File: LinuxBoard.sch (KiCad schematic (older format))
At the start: 0 parts

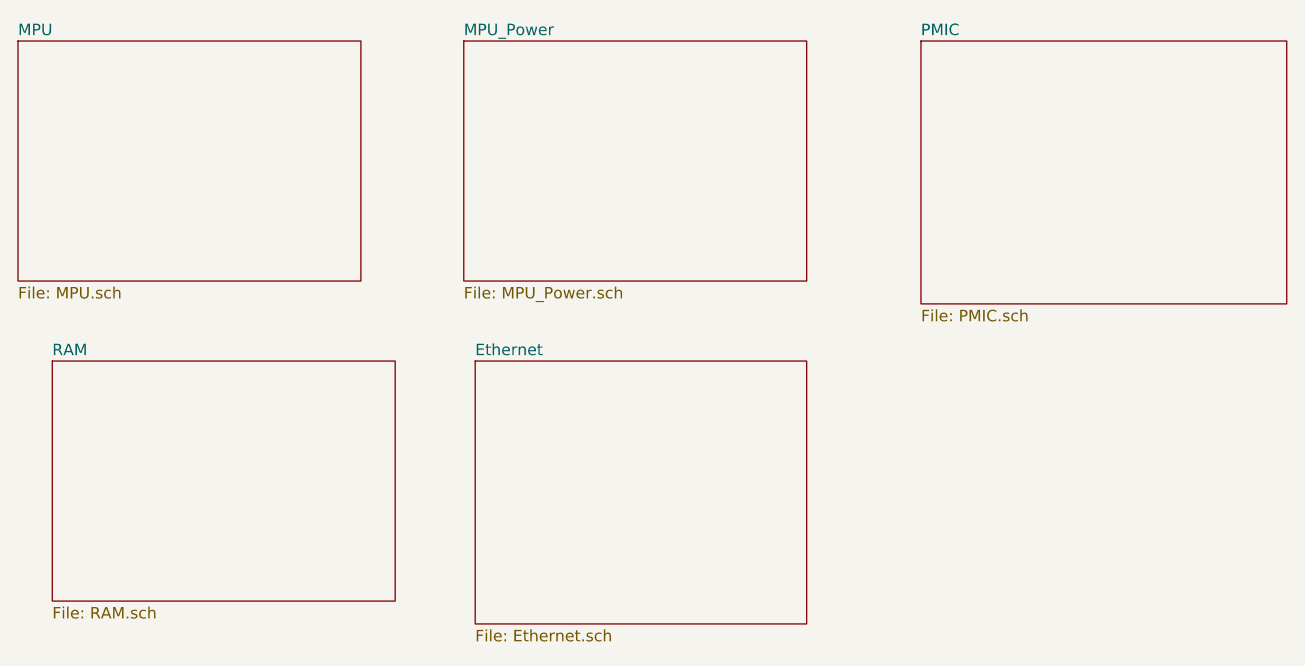
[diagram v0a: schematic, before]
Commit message: Complete ethernet and PMIC circuitry
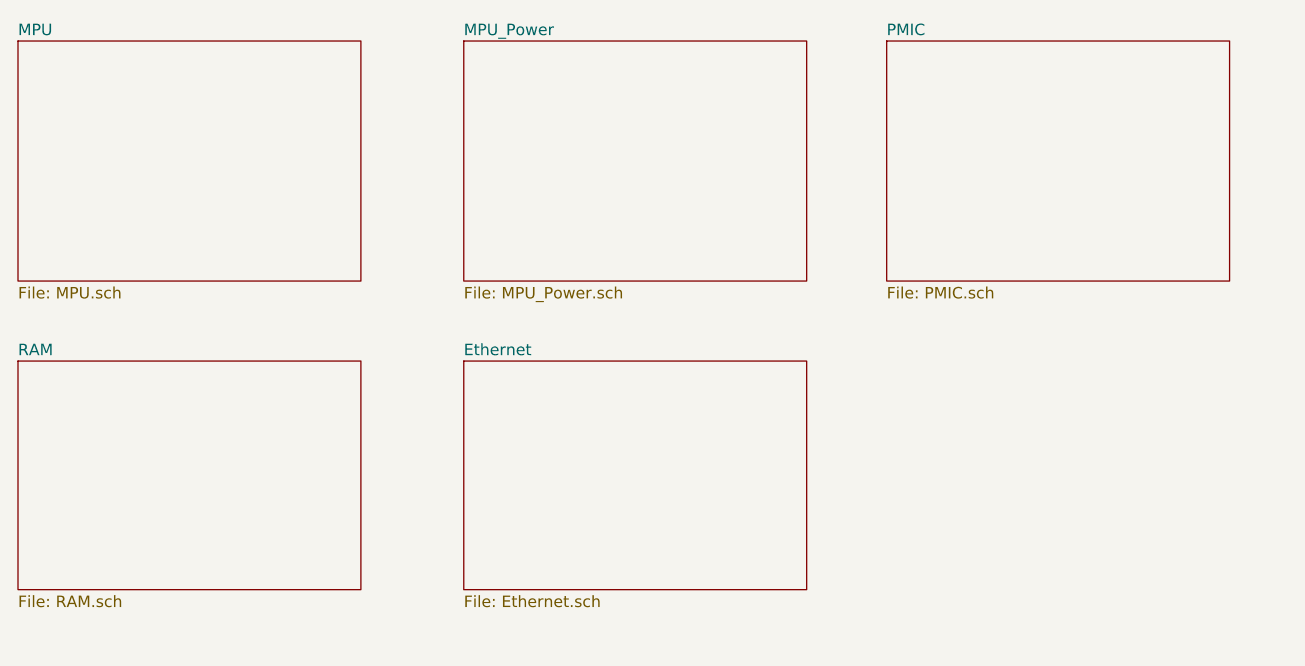
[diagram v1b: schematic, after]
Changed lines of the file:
@@
 $EndSheet
 $Sheet
-S 3300 3500 1500 1050
+S 3150 3500 1500 1000
 U 60172A77
 F0 "RAM" 50
@@
 $EndSheet
 $Sheet
-S 5150 3500 1450 1150
+S 5100 3500 1500 1000
 U 60172AD8
 F0 "Ethernet" 50
@@
 $EndSheet
 $Sheet
-S 7100 2100 1600 1150
+S 6950 2100 1500 1050
 U 60172B24
 F0 "PMIC" 50

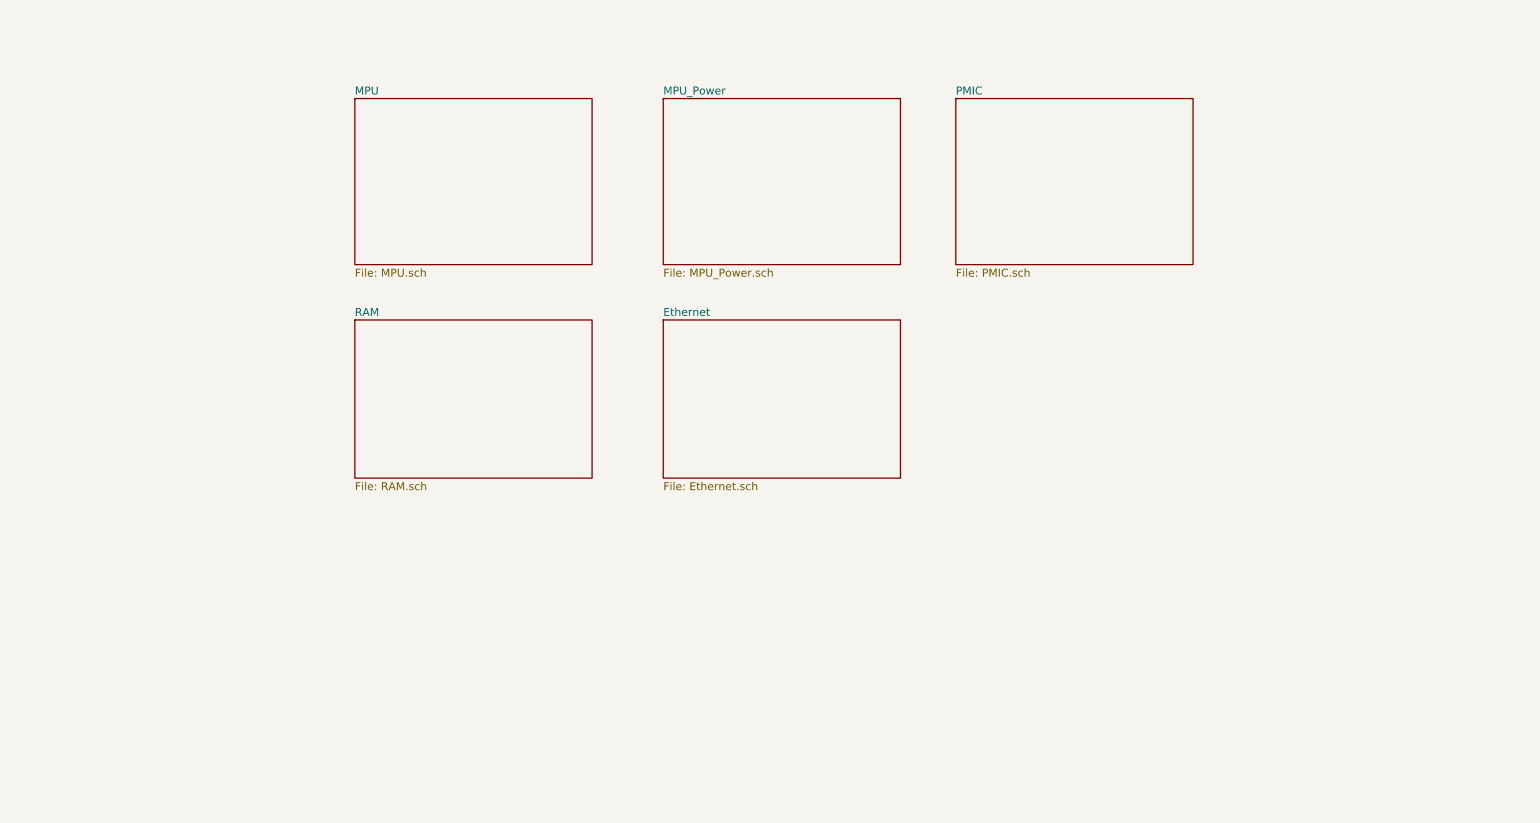
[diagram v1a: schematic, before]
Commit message: Complete gpio selection, tidy sheets
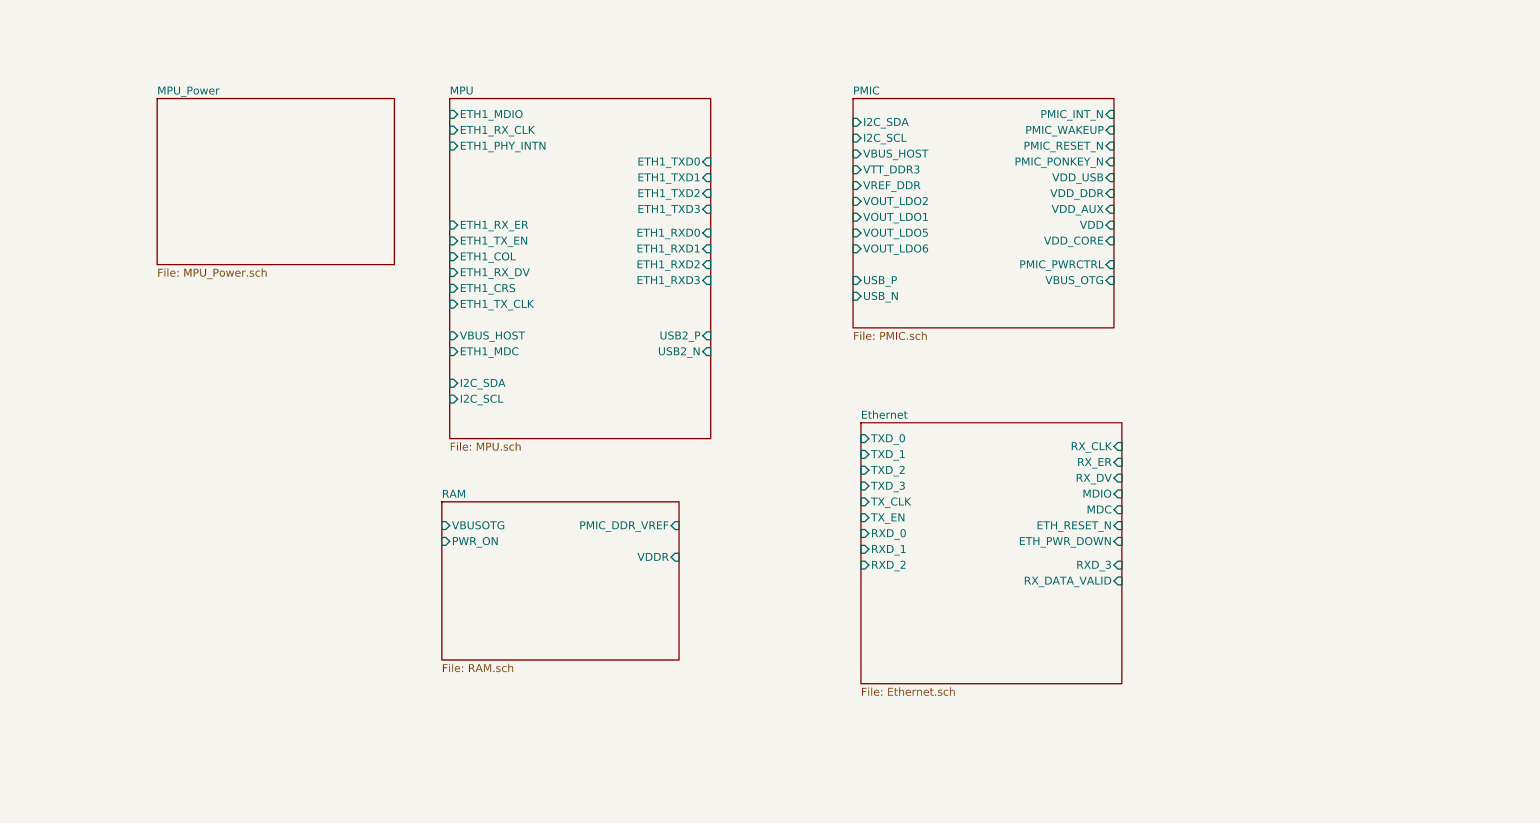
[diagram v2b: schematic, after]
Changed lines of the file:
@@
 $EndDescr
 $Sheet
-S 3150 2100 1500 1050
+S 3750 2100 1650 2150
 U 601728C0
 F0 "MPU" 50
 F1 "MPU.sch" 50
+F2 "ETH1_CRS" I L 3750 3300 50
+F3 "ETH1_RX_CLK" I L 3750 2300 50
+F4 "ETH1_MDIO" I L 3750 2200 50
+F5 "ETH1_COL" I L 3750 3100 50
+F6 "ETH1_RX_DV" I L 3750 3200 50
+F7 "ETH1_RXD2" I R 5400 3150 50
+F8 "ETH1_RXD3" I R 5400 3250 50
+F9 "ETH1_RX_ER" I L 3750 2900 50
+F10 "ETH1_TX_EN" I L 3750 3000 50
+F11 "ETH1_TXD1" I R 5400 2600 50
+F12 "ETH1_MDC" I L 3750 3700 50
+F13 "ETH1_TXD2" I R 5400 2700 50
+F14 "ETH1_TX_CLK" I L 3750 3400 50
+F15 "ETH1_RXD0" I R 5400 2950 50
+F16 "ETH1_RXD1" I R 5400 3050 50
+F17 "ETH1_TXD3" I R 5400 2800 50
+F18 "ETH1_PHY_INTN" I L 3750 2400 50
+F19 "ETH1_TXD0" I R 5400 2500 50
+F20 "I2C_SCL" I L 3750 4000 50
+F21 "I2C_SDA" I L 3750 3900 50
+F22 "VBUS_HOST" I L 3750 3600 50
+F23 "USB2_P" I R 5400 3600 50
+F24 "USB2_N" I R 5400 3700 50
 $EndSheet
 $Sheet
-S 5100 2100 1500 1050
+S 1900 2100 1500 1050
 U 601728E9
 F0 "MPU_Power" 50
@@
 $EndSheet
 $Sheet
-S 3150 3500 1500 1000
+S 3700 4650 1500 1000
 U 60172A77
 F0 "RAM" 50
 F1 "RAM.sch" 50
+F2 "VDDR" I R 5200 5000 50
+F3 "PMIC_DDR_VREF" I R 5200 4800 50
+F4 "PWR_ON" I L 3700 4900 50
+F5 "VBUSOTG" I L 3700 4800 50
 $EndSheet
 $Sheet
-S 5100 3500 1500 1000
+S 6350 4150 1650 1650
 U 60172AD8
 F0 "Ethernet" 50
 F1 "Ethernet.sch" 50
+F2 "TXD_0" I L 6350 4250 50
+F3 "TXD_1" I L 6350 4350 50
+F4 "TXD_2" I L 6350 4450 50
+F5 "TXD_3" I L 6350 4550 50
+F6 "TX_CLK" I L 6350 4650 50
+F7 "TX_EN" I L 6350 4750 50
+F8 "RXD_0" I L 6350 4850 50
+F9 "RXD_1" I L 6350 4950 50
+F10 "RXD_2" I L 6350 5050 50
+F11 "RXD_3" I R 8000 5050 50
+F12 "RX_CLK" I R 8000 4300 50
+F13 "RX_ER" I R 8000 4400 50
+F14 "RX_DV" I R 8000 4500 50
+F15 "MDIO" I R 8000 4600 50
+F16 "MDC" I R 8000 4700 50
+F17 "ETH_RESET_N" I R 8000 4800 50
+F18 "ETH_PWR_DOWN" I R 8000 4900 50
+F19 "RX_DATA_VALID" I R 8000 5150 50
 $EndSheet
 $Sheet
-S 6950 2100 1500 1050
+S 6300 2100 1650 1450
 U 60172B24
 F0 "PMIC" 50
 F1 "PMIC.sch" 50
+F2 "I2C_SDA" I L 6300 2250 50
+F3 "I2C_SCL" I L 6300 2350 50
+F4 "VBUS_HOST" I L 6300 2450 50
+F5 "VTT_DDR3" I L 6300 2550 50
+F6 "VREF_DDR" I L 6300 2650 50
+F7 "VOUT_LDO2" I L 6300 2750 50
+F8 "VOUT_LDO1" I L 6300 2850 50
+F9 "VOUT_LDO5" I L 6300 2950 50
+F10 "VOUT_LDO6" I L 6300 3050 50
+F11 "VDD_CORE" I R 7950 3000 50
+F12 "VDD" I R 7950 2900 50
+F13 "VDD_AUX" I R 7950 2800 50
+F14 "VDD_DDR" I R 7950 2700 50
+F15 "VDD_USB" I R 7950 2600 50
+F16 "PMIC_PONKEY_N" I R 7950 2500 50
+F17 "PMIC_RESET_N" I R 7950 2400 50
+F18 "PMIC_WAKEUP" I R 7950 2300 50
+F19 "PMIC_INT_N" I R 7950 2200 50
+F20 "PMIC_PWRCTRL" I R 7950 3150 50
+F21 "VBUS_OTG" I R 7950 3250 50
+F22 "USB_P" I L 6300 3250 50
+F23 "USB_N" I L 6300 3350 50
 $EndSheet
 $EndSCHEMATC

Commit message: Add DC barrel connector for alternate power supply
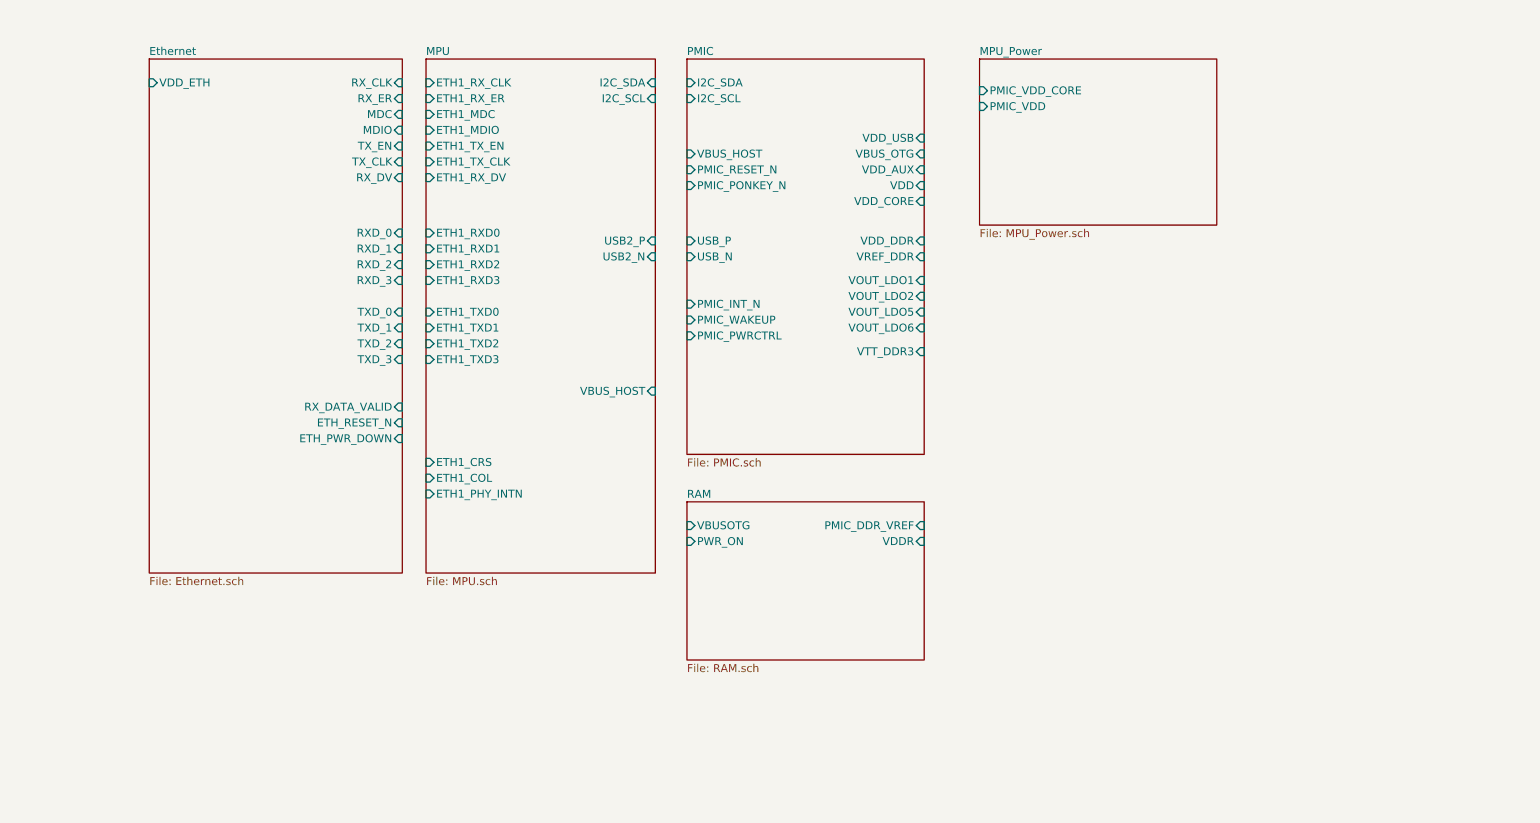
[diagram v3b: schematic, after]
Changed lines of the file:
@@
 $EndDescr
 $Sheet
-S 3750 2100 1650 2150
+S 3600 1850 1450 3250
 U 601728C0
 F0 "MPU" 50
 F1 "MPU.sch" 50
-F2 "ETH1_CRS" I L 3750 3300 50
-F3 "ETH1_RX_CLK" I L 3750 2300 50
-F4 "ETH1_MDIO" I L 3750 2200 50
-F5 "ETH1_COL" I L 3750 3100 50
-F6 "ETH1_RX_DV" I L 3750 3200 50
-F7 "ETH1_RXD2" I R 5400 3150 50
-F8 "ETH1_RXD3" I R 5400 3250 50
-F9 "ETH1_RX_ER" I L 3750 2900 50
-F10 "ETH1_TX_EN" I L 3750 3000 50
-F11 "ETH1_TXD1" I R 5400 2600 50
-F12 "ETH1_MDC" I L 3750 3700 50
-F13 "ETH1_TXD2" I R 5400 2700 50
-F14 "ETH1_TX_CLK" I L 3750 3400 50
-F15 "ETH1_RXD0" I R 5400 2950 50
-F16 "ETH1_RXD1" I R 5400 3050 50
-F17 "ETH1_TXD3" I R 5400 2800 50
-F18 "ETH1_PHY_INTN" I L 3750 2400 50
-F19 "ETH1_TXD0" I R 5400 2500 50
-F20 "I2C_SCL" I L 3750 4000 50
-F21 "I2C_SDA" I L 3750 3900 50
-F22 "VBUS_HOST" I L 3750 3600 50
-F23 "USB2_P" I R 5400 3600 50
-F24 "USB2_N" I R 5400 3700 50
+F2 "ETH1_CRS" I L 3600 4400 50
+F3 "ETH1_RX_CLK" I L 3600 2000 50
+F4 "ETH1_MDIO" I L 3600 2300 50
+F5 "ETH1_COL" I L 3600 4500 50
+F6 "ETH1_RX_DV" I L 3600 2600 50
+F7 "ETH1_RXD2" I L 3600 3150 50
+F8 "ETH1_RXD3" I L 3600 3250 50
+F9 "ETH1_RX_ER" I L 3600 2100 50
+F10 "ETH1_TX_EN" I L 3600 2400 50
+F11 "ETH1_TXD1" I L 3600 3550 50
+F12 "ETH1_MDC" I L 3600 2200 50
+F13 "ETH1_TXD2" I L 3600 3650 50
+F14 "ETH1_TX_CLK" I L 3600 2500 50
+F15 "ETH1_RXD0" I L 3600 2950 50
+F16 "ETH1_RXD1" I L 3600 3050 50
+F17 "ETH1_TXD3" I L 3600 3750 50
+F18 "ETH1_PHY_INTN" I L 3600 4600 50
+F19 "ETH1_TXD0" I L 3600 3450 50
+F20 "I2C_SCL" I R 5050 2100 50
+F21 "I2C_SDA" I R 5050 2000 50
+F22 "VBUS_HOST" I R 5050 3950 50
+F23 "USB2_P" I R 5050 3000 50
+F24 "USB2_N" I R 5050 3100 50
 $EndSheet
 $Sheet
-S 1900 2100 1500 1050
+S 7100 1850 1500 1050
 U 601728E9
 F0 "MPU_Power" 50
 F1 "MPU_Power.sch" 50
+F2 "PMIC_VDD" I L 7100 2150 50
+F3 "PMIC_VDD_CORE" I L 7100 2050 50
 $EndSheet
 $Sheet
-S 3700 4650 1500 1000
+S 5250 4650 1500 1000
 U 60172A77
 F0 "RAM" 50
 F1 "RAM.sch" 50
-F2 "VDDR" I R 5200 5000 50
-F3 "PMIC_DDR_VREF" I R 5200 4800 50
-F4 "PWR_ON" I L 3700 4900 50
-F5 "VBUSOTG" I L 3700 4800 50
+F2 "VDDR" I R 6750 4900 50
+F3 "PMIC_DDR_VREF" I R 6750 4800 50
+F4 "PWR_ON" I L 5250 4900 50
+F5 "VBUSOTG" I L 5250 4800 50
 $EndSheet
 $Sheet
-S 6350 4150 1650 1650
+S 5250 1850 1500 2500
+U 60172B24
+F0 "PMIC" 50
+F1 "PMIC.sch" 50
+F2 "I2C_SDA" I L 5250 2000 50
+F3 "I2C_SCL" I L 5250 2100 50
+F4 "VBUS_HOST" I L 5250 2450 50
+F5 "VTT_DDR3" I R 6750 3700 50
+F6 "VREF_DDR" I R 6750 3100 50
+F7 "VOUT_LDO2" I R 6750 3350 50
+F8 "VOUT_LDO1" I R 6750 3250 50
+F9 "VOUT_LDO5" I R 6750 3450 50
+F10 "VOUT_LDO6" I R 6750 3550 50
+F11 "VDD_CORE" I R 6750 2750 50
+F12 "VDD" I R 6750 2650 50
+F13 "VDD_AUX" I R 6750 2550 50
+F14 "VDD_DDR" I R 6750 3000 50
+F15 "VDD_USB" I R 6750 2350 50
+F16 "PMIC_PONKEY_N" I L 5250 2650 50
+F17 "PMIC_RESET_N" I L 5250 2550 50
+F18 "PMIC_WAKEUP" I L 5250 3500 50
+F19 "PMIC_INT_N" I L 5250 3400 50
+F20 "PMIC_PWRCTRL" I L 5250 3600 50
+F21 "VBUS_OTG" I R 6750 2450 50
+F22 "USB_P" I L 5250 3000 50
+F23 "USB_N" I L 5250 3100 50
+$EndSheet
+$Sheet
+S 1850 1850 1600 3250
 U 60172AD8
 F0 "Ethernet" 50
 F1 "Ethernet.sch" 50
-F2 "TXD_0" I L 6350 4250 50
-F3 "TXD_1" I L 6350 4350 50
-F4 "TXD_2" I L 6350 4450 50
-F5 "TXD_3" I L 6350 4550 50
-F6 "TX_CLK" I L 6350 4650 50
-F7 "TX_EN" I L 6350 4750 50
-F8 "RXD_0" I L 6350 4850 50
-F9 "RXD_1" I L 6350 4950 50
-F10 "RXD_2" I L 6350 5050 50
-F11 "RXD_3" I R 8000 5050 50
-F12 "RX_CLK" I R 8000 4300 50
-F13 "RX_ER" I R 8000 4400 50
-F14 "RX_DV" I R 8000 4500 50
-F15 "MDIO" I R 8000 4600 50
-F16 "MDC" I R 8000 4700 50
-F17 "ETH_RESET_N" I R 8000 4800 50
-F18 "ETH_PWR_DOWN" I R 8000 4900 50
-F19 "RX_DATA_VALID" I R 8000 5150 50
-$EndSheet
-$Sheet
-S 6300 2100 1650 1450
-U 60172B24
-F0 "PMIC" 50
-F1 "PMIC.sch" 50
-F2 "I2C_SDA" I L 6300 2250 50
-F3 "I2C_SCL" I L 6300 2350 50
-F4 "VBUS_HOST" I L 6300 2450 50
-F5 "VTT_DDR3" I L 6300 2550 50
-F6 "VREF_DDR" I L 6300 2650 50
-F7 "VOUT_LDO2" I L 6300 2750 50
-F8 "VOUT_LDO1" I L 6300 2850 50
-F9 "VOUT_LDO5" I L 6300 2950 50
-F10 "VOUT_LDO6" I L 6300 3050 50
-F11 "VDD_CORE" I R 7950 3000 50
-F12 "VDD" I R 7950 2900 50
-F13 "VDD_AUX" I R 7950 2800 50
-F14 "VDD_DDR" I R 7950 2700 50
-F15 "VDD_USB" I R 7950 2600 50
-F16 "PMIC_PONKEY_N" I R 7950 2500 50
-F17 "PMIC_RESET_N" I R 7950 2400 50
-F18 "PMIC_WAKEUP" I R 7950 2300 50
-F19 "PMIC_INT_N" I R 7950 2200 50
-F20 "PMIC_PWRCTRL" I R 7950 3150 50
-F21 "VBUS_OTG" I R 7950 3250 50
-F22 "USB_P" I L 6300 3250 50
-F23 "USB_N" I L 6300 3350 50
+F2 "TXD_0" I R 3450 3450 50
+F3 "TXD_1" I R 3450 3550 50
+F4 "TXD_2" I R 3450 3650 50
+F5 "TXD_3" I R 3450 3750 50
+F6 "TX_CLK" I R 3450 2500 50
+F7 "TX_EN" I R 3450 2400 50
+F8 "RXD_0" I R 3450 2950 50
+F9 "RXD_1" I R 3450 3050 50
+F10 "RXD_2" I R 3450 3150 50
+F11 "RXD_3" I R 3450 3250 50
+F12 "RX_CLK" I R 3450 2000 50
+F13 "RX_ER" I R 3450 2100 50
+F14 "RX_DV" I R 3450 2600 50
+F15 "MDIO" I R 3450 2300 50
+F16 "MDC" I R 3450 2200 50
+F17 "ETH_RESET_N" I R 3450 4150 50
+F18 "ETH_PWR_DOWN" I R 3450 4250 50
+F19 "RX_DATA_VALID" I R 3450 4050 50
+F20 "VDD_ETH" I L 1850 2000 50
 $EndSheet
 $EndSCHEMATC
